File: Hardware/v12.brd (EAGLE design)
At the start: 50 x 50 mm, 85 parts, among them J1 22-27-2081-08, J2 22-27-2031-03

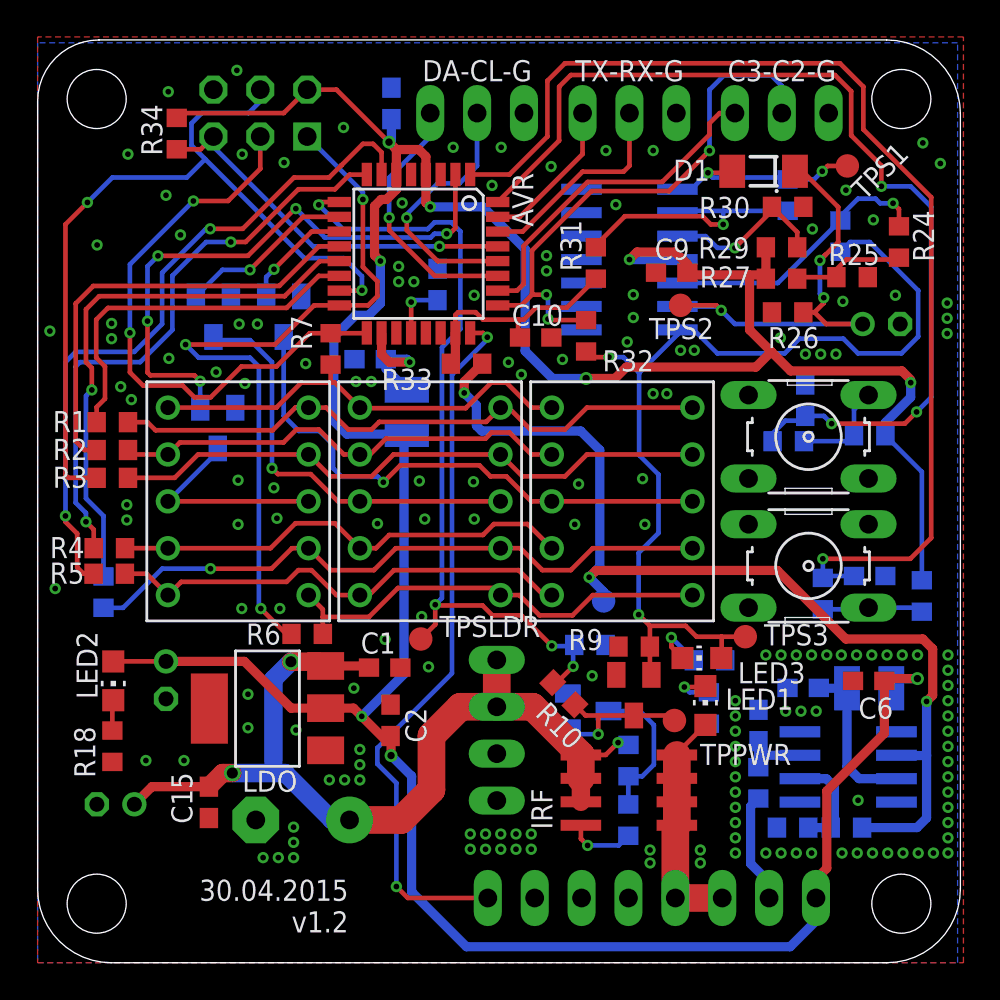
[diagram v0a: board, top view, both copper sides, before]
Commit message: reworked the schematic and had to reconnect some signals in the layout. no substantial changes
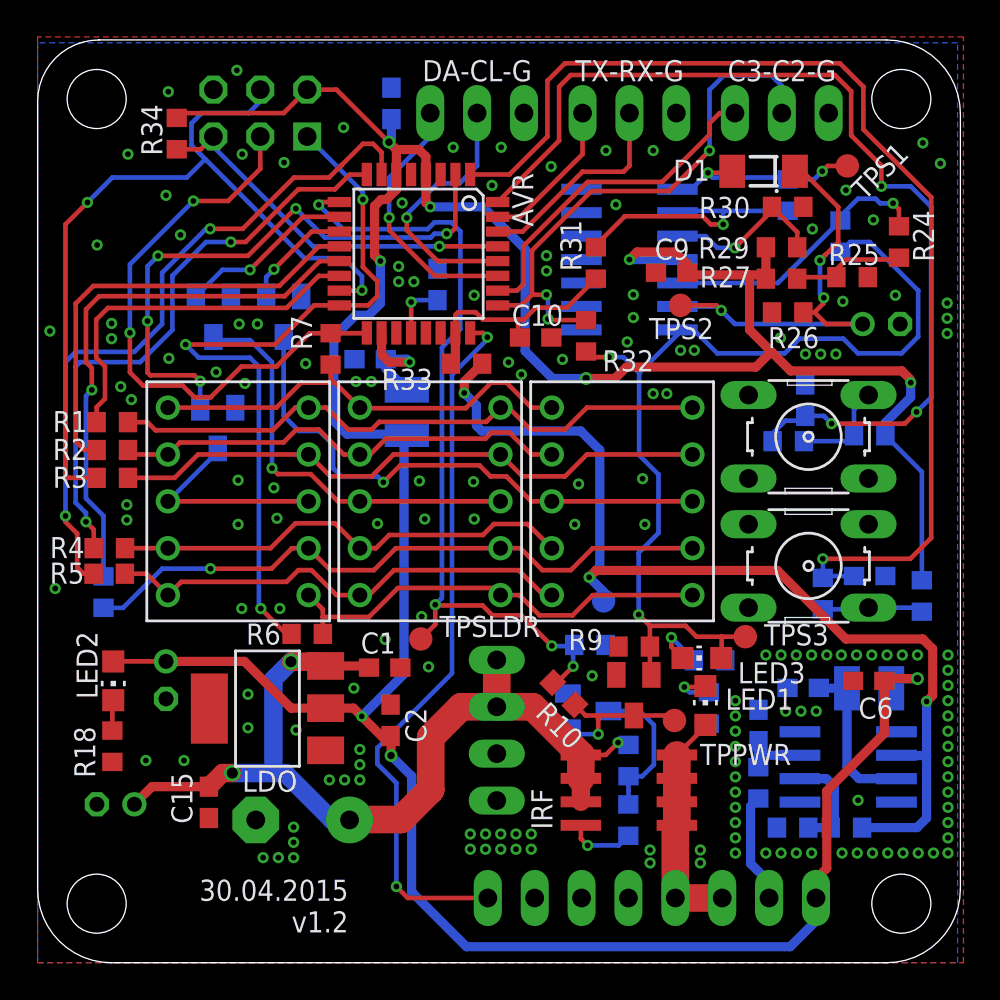
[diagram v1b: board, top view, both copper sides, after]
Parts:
- R32: value 0 n.m. -> 1k n.m.
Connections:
- net N$32 renamed P-FET_GATE
